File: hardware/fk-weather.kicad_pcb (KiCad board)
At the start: 2 copper layers, 28.7 x 107.4 mm, 78 parts, among them J1 MICRO-USB, J2 CONN_01X03, J6 CONN-HDR-2x5, M1 MOUNT_HOLE, M2 MOUNT_HOLE, M3 MOUNT_HOLE, M4 MOUNT_HOLE, P101 CONN_01X05, Q1 2N7002LT1G, Q2 2N7002LT1G, Q3 2N7002LT1G, SW1 SPNO, U1 ATSAMD21G18A-AU, U101 TSL2591, U102 MPL3115A2, U103 BNO055, U104 SHT31, U2 MCP1700T-XXX2E, U3 MAX4466, Y1 FC-135, Y101 FC-135

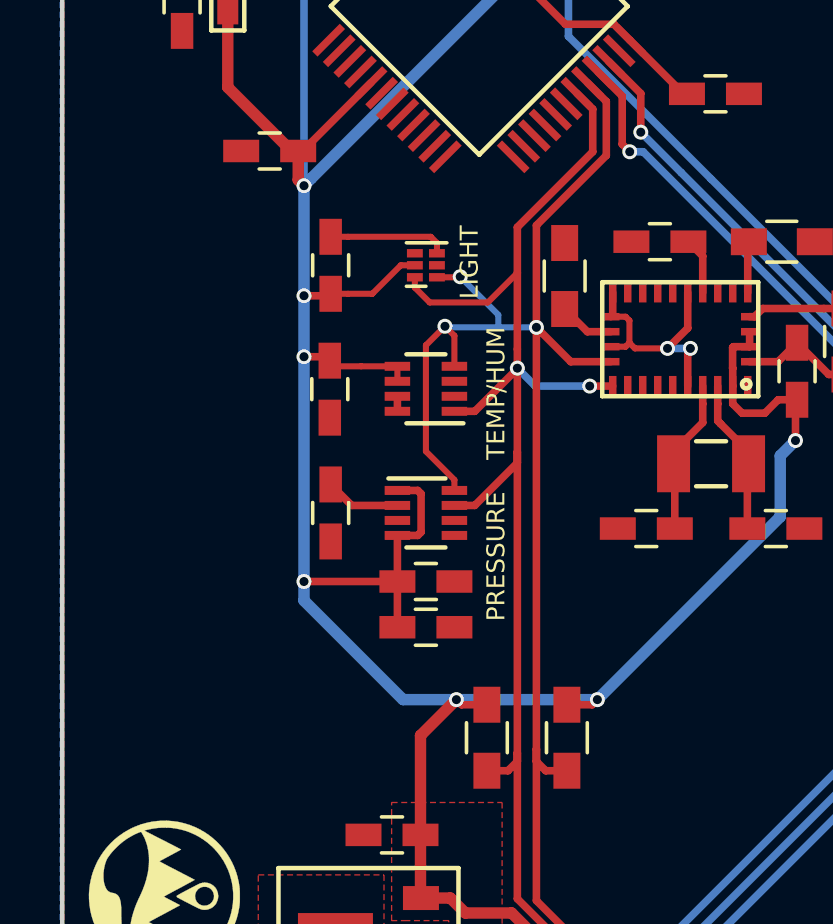
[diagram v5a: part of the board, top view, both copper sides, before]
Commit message: Fixing footprints for light and pressure.
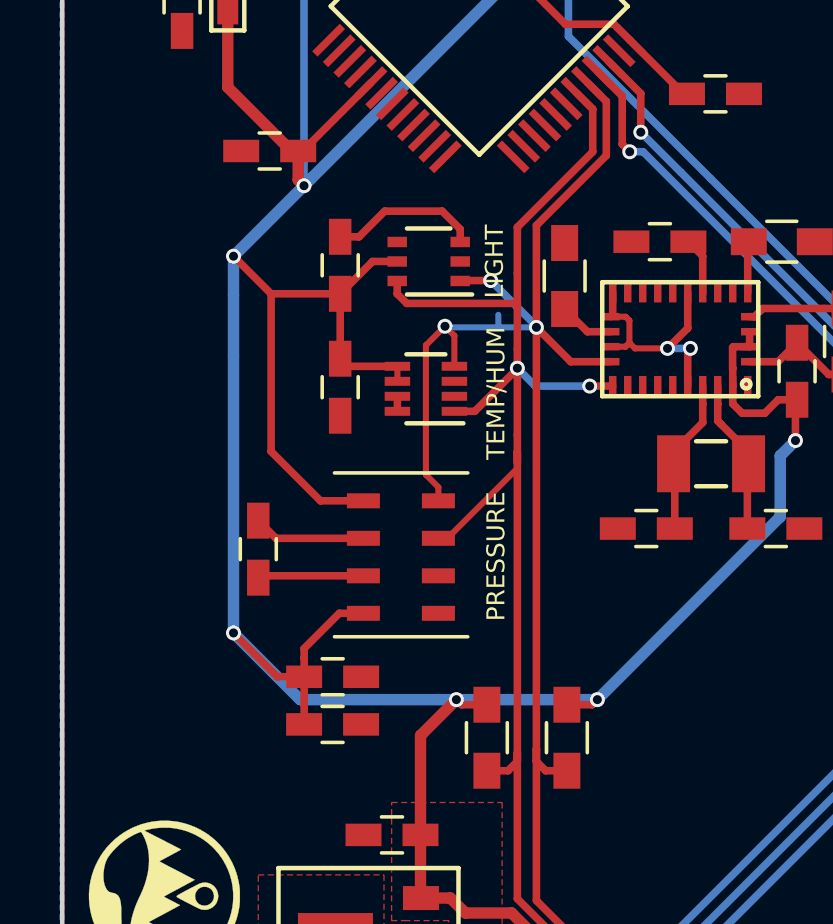
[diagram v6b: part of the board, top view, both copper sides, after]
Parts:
- L3, L4: value ? -> 100 to 1k above 10MHz
- U101: footprint Housings_DFN_QFN:DFN-6-1.3x1.2mm_Pitch0.4mm -> Housings_DFN_QFN:DFN-6-1EP_2x2mm_Pitch0.65mm
- U102: footprint Housings_DFN_QFN:DFN-8_2x2mm_Pitch0.5mm -> conservify:DFN-8-1EP_5x2.55mm_Pitch1.25mm_98ASA002260D
- moved C103 4.49 mm to (134.8, 130.1)
- moved C104 4.44 mm to (134.8, 128.5)
- moved C102 2.70 mm to (132.3, 124.3)
- moved U102 1.55 mm to (137.4, 124.5)
- moved C109 0.35 mm to (135.1, 118.9)
- moved C101 0.32 mm to (135.1, 114.8)
- moved U101 0.16 mm to (138.0, 114.7)
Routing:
- net 3V3: track 226.2 -> 241.2 mm, vias 14 -> 13
- net GND: track 26.3 -> 30.7 mm
- net /SDA: track 56.7 -> 58.9 mm
- net Net-(C102-Pad1): track 2.51 -> 3.75 mm
- net /SCL: track 65.3 -> 66.1 mm

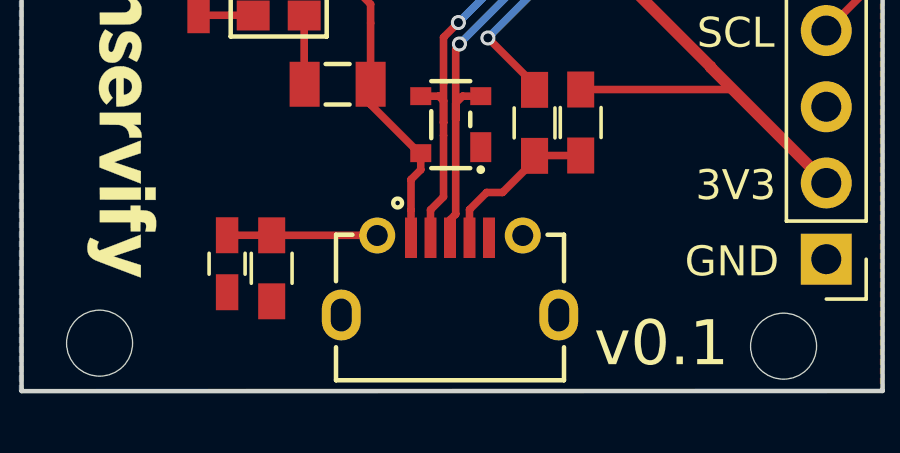
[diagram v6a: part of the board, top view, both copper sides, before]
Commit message: Fixing USB oval drills.
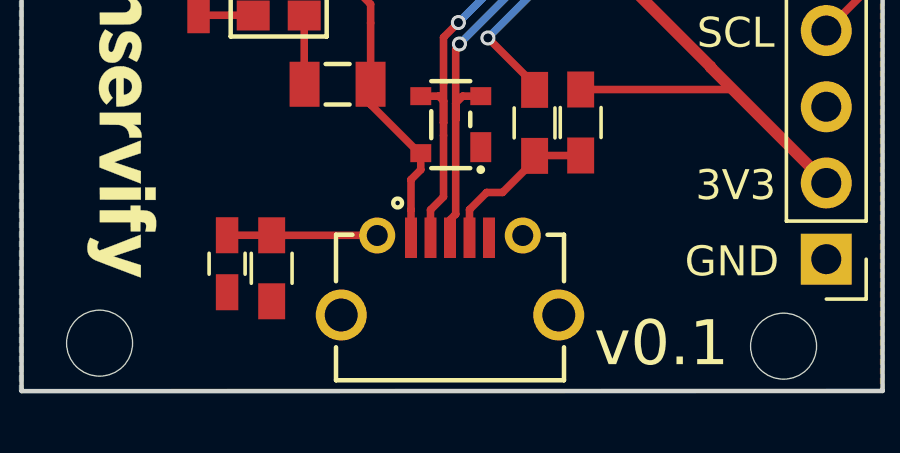
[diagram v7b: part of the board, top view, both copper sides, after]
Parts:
- J1: footprint RocketScreamKicadLibrary:MICRO-USB -> conservify:MICRO-USB
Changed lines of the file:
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@@
     (links 170)
     (no_connects 0)
-    (area 106.352905 47.724999 165.914286 159.377948)
+    (area 125.724999 47.724999 154.575001 155.275001)
     (thickness 1.6)
     (drawings 14)
@@
     (47 F.CrtYd user)
     (48 B.Fab user hide)
-    (49 F.Fab user hide)
+    (49 F.Fab user)
   )
   (setup
@@
       (net 74 VUSB))
   )
-  (module RocketScreamKicadLibrary:MICRO-USB (layer F.Cu)
-    (at 140.081 151.5364)
-    (tags MICRO-USB)
-    (fp_text reference J1 (at 0 -3.556) (layer F.SilkS) hide
-      (effects (font (size 1 1) (thickness 0.15)))
-    )
-    (fp_text value MICRO-USB (at 0 4.318) (layer F.Fab)
-      (effects (font (size 1 1) (thickness 0.15)))
-    )
-    (fp_line (start -4.55 -2.4) (end -4.55 3.45) (layer F.CrtYd) (width 0.05))
-    (fp_line (start -4.55 3.45) (end 4.55 3.45) (layer F.CrtYd) (width 0.05))
-    (fp_line (start 4.55 3.45) (end 4.55 -2.4) (layer F.CrtYd) (width 0.05))
-    (fp_line (start 4.55 -2.4) (end -4.55 -2.4) (layer F.CrtYd) (width 0.05))
-    (fp_circle (center -1.746 -2.608) (end -1.796 -2.658) (layer F.SilkS) (width 0.3))
-    (fp_line (start 3.8 0) (end 3.8 -1.55) (layer F.SilkS) (width 0.15))
-    (fp_line (start 3.8 -1.55) (end 3.25 -1.55) (layer F.SilkS) (width 0.15))
-    (fp_line (start -3.8 0) (end -3.8 -1.55) (layer F.SilkS) (width 0.15))
-    (fp_line (start -3.8 -1.55) (end -3.25 -1.55) (layer F.SilkS) (width 0.15))
-    (fp_line (start 3.8 2.2) (end 3.8 3.3) (layer F.SilkS) (width 0.15))
-    (fp_line (start -3.8 3.3) (end -3.8 2.2) (layer F.SilkS) (width 0.15))
-    (fp_line (start -3.8 3.3) (end 3.8 3.3) (layer F.SilkS) (width 0.15))
-    (pad 1 smd rect (at -1.3 -1.45) (size 0.4 1.35) (layers F.Cu F.Paste F.Mask)
-      (net 74 VUSB))
-    (pad 2 smd rect (at -0.65 -1.45) (size 0.4 1.35) (layers F.Cu F.Paste F.Mask)
-      (net 47 /USB-))
-    (pad 3 smd rect (at 0 -1.45) (size 0.4 1.35) (layers F.Cu F.Paste F.Mask)
-      (net 48 /USB+))
-    (pad 4 smd rect (at 0.65 -1.45) (size 0.4 1.35) (layers F.Cu F.Paste F.Mask)
-      (net 75 "Net-(J1-Pad4)"))
-    (pad 5 smd rect (at 1.3 -1.45) (size 0.4 1.35) (layers F.Cu F.Paste F.Mask)
-      (net 1 GND))
-    (pad 6 thru_hole circle (at -2.425 -1.525) (size 1.2 1.2) (drill 0.7) (layers *.Cu *.Mask F.SilkS)
-      (net 73 "Net-(C10-Pad1)"))
-    (pad 7 thru_hole circle (at 2.425 -1.525) (size 1.2 1.2) (drill 0.7) (layers *.Cu *.Mask F.SilkS)
-      (net 76 "Net-(J1-Pad7)"))
-    (pad 8 thru_hole oval (at -3.625 1.125) (size 1.3 1.7) (drill oval 0.7 1.1) (layers *.Cu *.Mask F.SilkS)
-      (net 77 "Net-(J1-Pad8)"))
-    (pad 9 thru_hole oval (at 3.625 1.125) (size 1.3 1.7) (drill oval 0.7 1.1) (layers *.Cu *.Mask F.SilkS)
-      (net 78 "Net-(J1-Pad9)"))
-  )
   (module RocketScreamKicadLibrary:IND-0603 (layer F.Cu)
     (at 134.370749 142.678455)
@@
     )
   )
+  (module conservify:MICRO-USB (layer F.Cu)
+    (at 140.081 151.5364)
+    (tags MICRO-USB)
+    (fp_text reference J1 (at -26.162 0) (layer F.SilkS) hide
+      (effects (font (size 0.8 0.8) (thickness 0.15)))
+    )
+    (fp_text value MICRO-USB (at 0 4.318) (layer F.Fab)
+      (effects (font (size 0.8 0.8) (thickness 0.15)))
+    )
+    (fp_line (start -4.55 -2.4) (end -4.55 3.45) (layer F.CrtYd) (width 0.05))
+    (fp_line (start -4.55 3.45) (end 4.55 3.45) (layer F.CrtYd) (width 0.05))
+    (fp_line (start 4.55 3.45) (end 4.55 -2.4) (layer F.CrtYd) (width 0.05))
+    (fp_line (start 4.55 -2.4) (end -4.55 -2.4) (layer F.CrtYd) (width 0.05))
+    (fp_circle (center -1.746 -2.608) (end -1.796 -2.658) (layer F.SilkS) (width 0.3))
+    (fp_line (start 3.8 0) (end 3.8 -1.55) (layer F.SilkS) (width 0.15))
+    (fp_line (start 3.8 -1.55) (end 3.25 -1.55) (layer F.SilkS) (width 0.15))
+    (fp_line (start -3.8 0) (end -3.8 -1.55) (layer F.SilkS) (width 0.15))
+    (fp_line (start -3.8 -1.55) (end -3.25 -1.55) (layer F.SilkS) (width 0.15))
+    (fp_line (start 3.8 2.2) (end 3.8 3.3) (layer F.SilkS) (width 0.15))
+    (fp_line (start -3.8 3.3) (end -3.8 2.2) (layer F.SilkS) (width 0.15))
+    (fp_line (start -3.8 3.3) (end 3.8 3.3) (layer F.SilkS) (width 0.15))
+    (pad 1 smd rect (at -1.3 -1.45) (size 0.4 1.35) (layers F.Cu F.Paste F.Mask)
+      (net 74 VUSB))
+    (pad 2 smd rect (at -0.65 -1.45) (size 0.4 1.35) (layers F.Cu F.Paste F.Mask)
+      (net 47 /USB-))
+    (pad 3 smd rect (at 0 -1.45) (size 0.4 1.35) (layers F.Cu F.Paste F.Mask)
+      (net 48 /USB+))
+    (pad 4 smd rect (at 0.65 -1.45) (size 0.4 1.35) (layers F.Cu F.Paste F.Mask)
+      (net 75 "Net-(J1-Pad4)"))
+    (pad 5 smd rect (at 1.3 -1.45) (size 0.4 1.35) (layers F.Cu F.Paste F.Mask)
+      (net 1 GND))
+    (pad 6 thru_hole circle (at -2.425 -1.525) (size 1.2 1.2) (drill 0.7) (layers *.Cu *.Mask F.Paste)
+      (net 73 "Net-(C10-Pad1)"))
+    (pad 7 thru_hole circle (at 2.425 -1.525) (size 1.2 1.2) (drill 0.7) (layers *.Cu *.Mask F.Paste)
+      (net 76 "Net-(J1-Pad7)"))
+    (pad 8 thru_hole circle (at -3.625 1.125) (size 1.7 1.7) (drill oval 1.1) (layers *.Cu *.Mask F.Paste)
+      (net 77 "Net-(J1-Pad8)"))
+    (pad 9 thru_hole circle (at 3.625 1.125) (size 1.7 1.7) (drill oval 1.1) (layers *.Cu *.Mask F.Paste)
+      (net 78 "Net-(J1-Pad9)"))
+  )
   (gr_text LIGHT (at 140.208 114.681 90) (layer F.SilkS)
     (effects (font (size 0.6 0.6) (thickness 0.15)))
@@
     (connect_pads (clearance 0.2032))
     (min_thickness 0.253)
-    (fill (arc_segments 32) (thermal_gap 0.254) (thermal_bridge_width 0.254) (smoothing chamfer))
+    (fill yes (arc_segments 32) (thermal_gap 0.254) (thermal_bridge_width 0.254) (smoothing chamfer))
     (polygon
       (pts
@@
     (connect_pads (clearance 0.2032))
     (min_thickness 0.253)
-    (fill (arc_segments 32) (thermal_gap 0.254) (thermal_bridge_width 0.254) (smoothing chamfer))
+    (fill yes (arc_segments 32) (thermal_gap 0.254) (thermal_bridge_width 0.254) (smoothing chamfer))
     (polygon
       (pts
@@
     (connect_pads (clearance 0.2032))
     (min_thickness 0.253)
-    (fill (arc_segments 32) (thermal_gap 0.254) (thermal_bridge_width 0.254) (smoothing chamfer))
+    (fill yes (arc_segments 32) (thermal_gap 0.254) (thermal_bridge_width 0.254) (smoothing chamfer))
     (polygon
       (pts
@@
     (connect_pads (clearance 0.2032))
     (min_thickness 0.253)
-    (fill (arc_segments 32) (thermal_gap 0.254) (thermal_bridge_width 0.254) (smoothing chamfer))
+    (fill yes (arc_segments 32) (thermal_gap 0.254) (thermal_bridge_width 0.254) (smoothing chamfer))
     (polygon
       (pts

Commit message: Arranging labels for printing out an assembly map.
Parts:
- L3, L4: value 100 to 1k above 10MHz -> WE-CBF
